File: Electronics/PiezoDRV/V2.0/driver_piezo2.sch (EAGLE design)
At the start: 37 parts, among them J1 RJ12STRAIGHT-ANALOG, T1 FMMT718

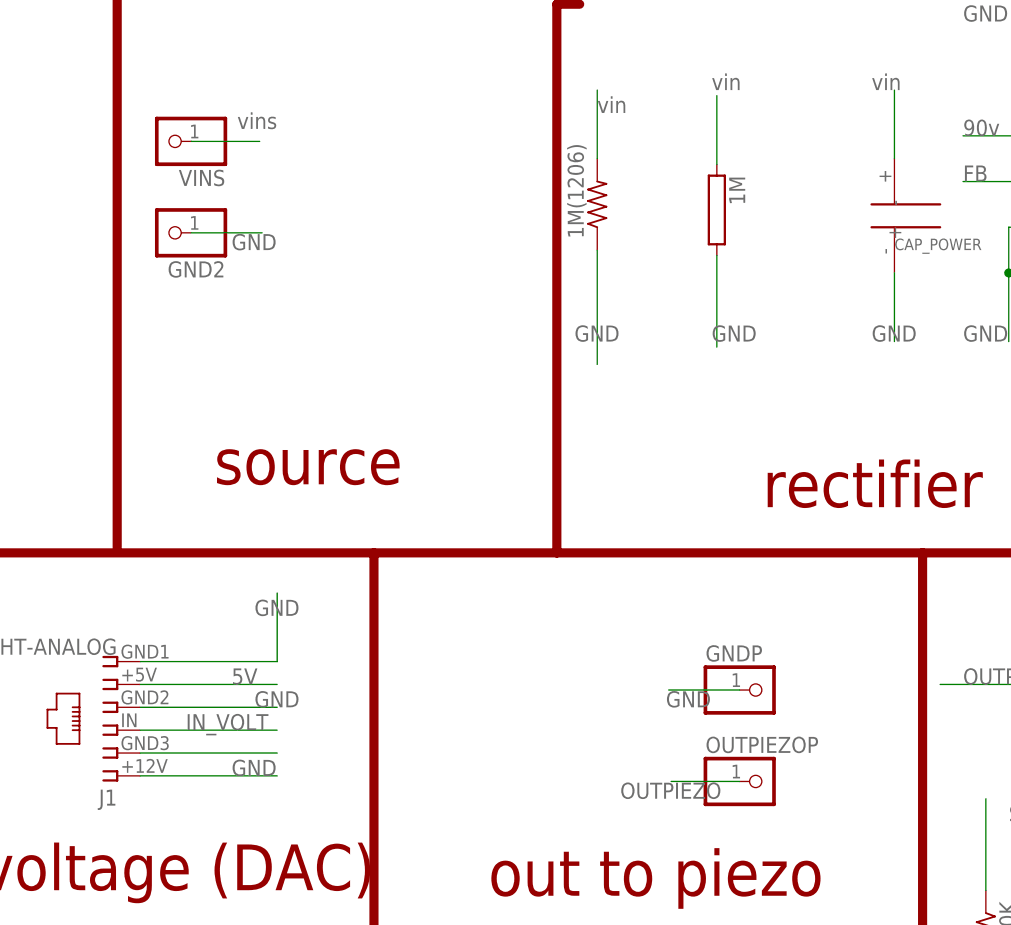
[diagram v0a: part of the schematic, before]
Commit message: corrections on piezo driver v2.0, generated gerbers
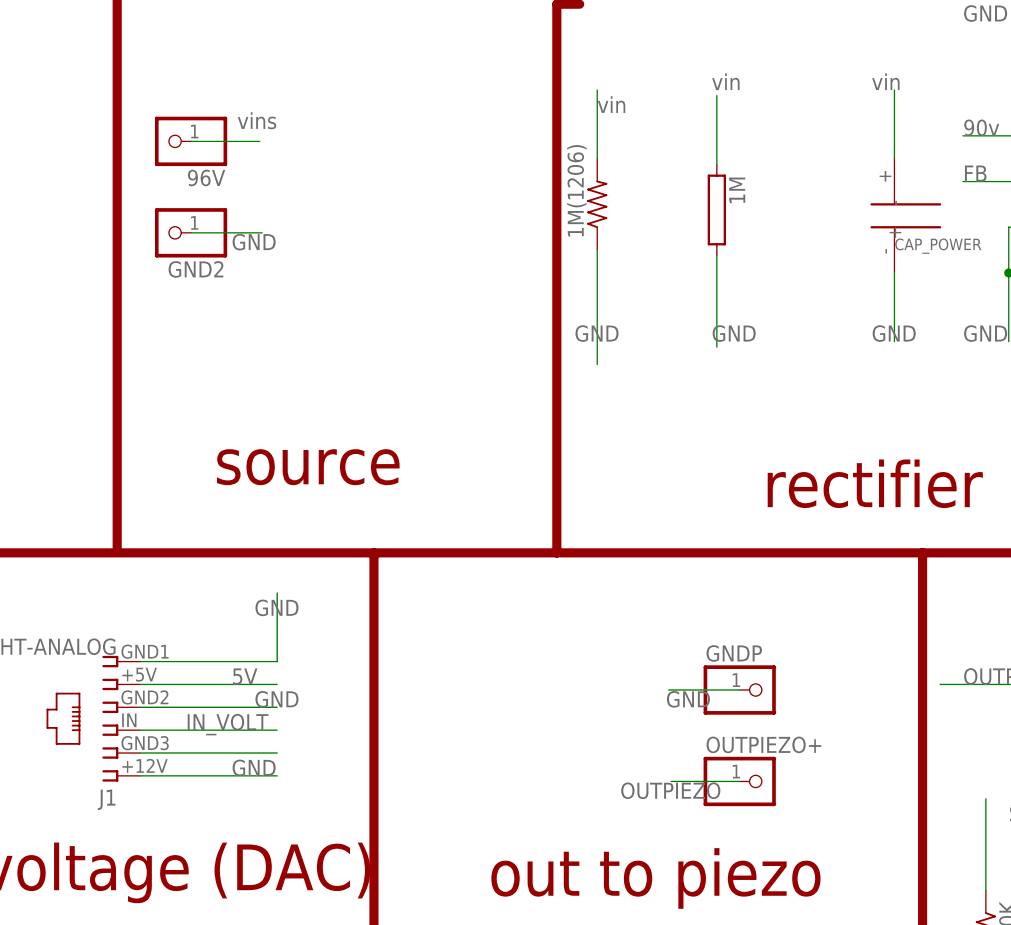
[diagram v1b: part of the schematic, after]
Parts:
- renumbered OUTPIEZOP to OUTPIEZO+, VINS to 96V
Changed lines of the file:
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@@
 <?xml version="1.0" encoding="utf-8"?>
 <!DOCTYPE eagle SYSTEM "eagle.dtd">
-<eagle version="7.0.0">
+<eagle version="7.1.0">
 <drawing>
 <settings>
@@
 <part name="1M" library="resistor-power" deviceset="R" device="CA0002"/>
 <part name="GNDP" library="pinhead" deviceset="PINHD-1X1" device=""/>
-<part name="OUTPIEZOP" library="pinhead" deviceset="PINHD-1X1" device=""/>
+<part name="OUTPIEZO+" library="pinhead" deviceset="PINHD-1X1" device=""/>
 <part name="GND2" library="pinhead" deviceset="PINHD-1X1" device=""/>
-<part name="VINS" library="pinhead" deviceset="PINHD-1X1" device=""/>
+<part name="96V" library="pinhead" deviceset="PINHD-1X1" device=""/>
 <part name="J1" library="lpatiny" deviceset="RJ12" device="STRAIGHT-ANALOG"/>
 <part name="CAP_POWER" library="PIEZO_LBR" deviceset="CAP200V" device="CAP200V"/>
@@
 <instance part="1M" gate="G$1" x="-19.73" y="52.72" rot="R270"/>
 <instance part="GNDP" gate="G$1" x="-14.65" y="-0.62"/>
-<instance part="OUTPIEZOP" gate="G$1" x="-14.65" y="-10.78"/>
+<instance part="OUTPIEZO+" gate="G$1" x="-14.65" y="-10.78"/>
 <instance part="GND2" gate="G$1" x="-80.69" y="50.18" rot="R180"/>
-<instance part="VINS" gate="G$1" x="-80.69" y="60.34" rot="R180"/>
+<instance part="96V" gate="G$1" x="-80.69" y="60.34" rot="R180"/>
 <instance part="J1" gate="G$1" x="-86.36" y="-5.08" rot="R180"/>
 <instance part="CAP_POWER" gate="G$1" x="-2.54" y="53.34"/>
@@
 <net name="OUT_PIEZO" class="0">
 <segment>
-<pinref part="OUTPIEZOP" gate="G$1" pin="1"/>
+<pinref part="OUTPIEZO+" gate="G$1" pin="1"/>
 <wire x1="-17.19" y1="-10.78" x2="-24.81" y2="-10.78" width="0.1524" layer="91"/>
 </segment>
@@
 </segment>
 <segment>
-<pinref part="VINS" gate="G$1" pin="1"/>
+<pinref part="96V" gate="G$1" pin="1"/>
 <wire x1="-78.15" y1="60.34" x2="-70.53" y2="60.34" width="0.1524" layer="91"/>
 </segment>
